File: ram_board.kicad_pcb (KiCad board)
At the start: 4 copper layers, 72.6 x 31.6 mm, 25 parts, among them J1 Bus, J2 PWR, SW1 Config, U1 CPU - Z84C0010AEG, U2 IS61LV5128AL-10TLI, U3 SST39VF040-70-4C-NHE, U4 74LVC2G240, X1 ASV-xxxMHz

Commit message: re-gridded
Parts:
- removed C5: 100nF, Capacitor_SMD:C_0603_1608Metric_Pad1.05x0.95mm_HandSolder
- removed R4, R5, R6, R7, R8, R9: 10K, Resistor_SMD:R_0603_1608Metric_Pad1.05x0.95mm_HandSolder
- removed SW1: Config, Button_Switch_SMD:SW_DIP_SPSTx06_Slide_KingTek_DSHP06TS_W7.62mm_P1.27mm
- X1: value ASV-xxxMHz -> ASV-20MHz
- renumbered C3 to C1, C1 to C2, C2 to C3, U2 to U1, U3 to U2, U1 to U3
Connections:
- C1 pad 1: +3V3 -> Net-(C1-Pad1)
- C2 pad 1: +3V3 -> Net-(C1-Pad1)
- C3 pad 1: +3V3 -> Net-(C1-Pad1)
- C4 pad 1: +3V3 -> Net-(C1-Pad1)
- J1 pad 2: /SW1_5 -> /~RESET
- J1 pad 3: /SW1_3 -> /CLK
- J1 pad 4: /SW1_4 -> /~BUSREQ
- J1 pad 5: /SW1_1 -> /~WAIT
- J1 pad 6: /SW1_2 -> /~IORQ
- J1 pad 8: /SW1_0 -> /~MREQ
- J2 pad 10: (no net) -> /5V
- J2 pad 5: (no net) -> /1V8
- J2 pad 6: (no net) -> /1V8
- J2 pad 7: +3V3 -> VCC
- J2 pad 8: +3V3 -> VCC
- J2 pad 9: (no net) -> /5V
- R1 pad 2: +3V3 -> VCC
- R2 pad 2: +3V3 -> VCC
- R3 pad 2: +3V3 -> VCC
- U1 pad 11: +3V3 -> VCC
- U1 pad 33: +3V3 -> VCC
- U2 pad 32: +3V3 -> VCC
- U3 pad 1: (no net) -> /CLK
- U3 pad 15: (no net) -> /~MREQ
- U3 pad 16: (no net) -> /~IORQ
- U3 pad 21: (no net) -> /~WAIT
- U3 pad 22: (no net) -> /~BUSREQ
- U3 pad 23: (no net) -> /~RESET
- U3 pad 6: (no net) -> VCC
- U4 pad 8: +3V3 -> VCC
- X1 pad 1: (no net) -> VCC
- X1 pad 2: (no net) -> GND
- X1 pad 3: (no net) -> /CLK
- X1 pad 4: (no net) -> VCC
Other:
- board text removed: "1"
- board text removed: "16"
- board text removed: "2"
- board text removed: "32"
- board text removed: "4"
- board text removed: "8"

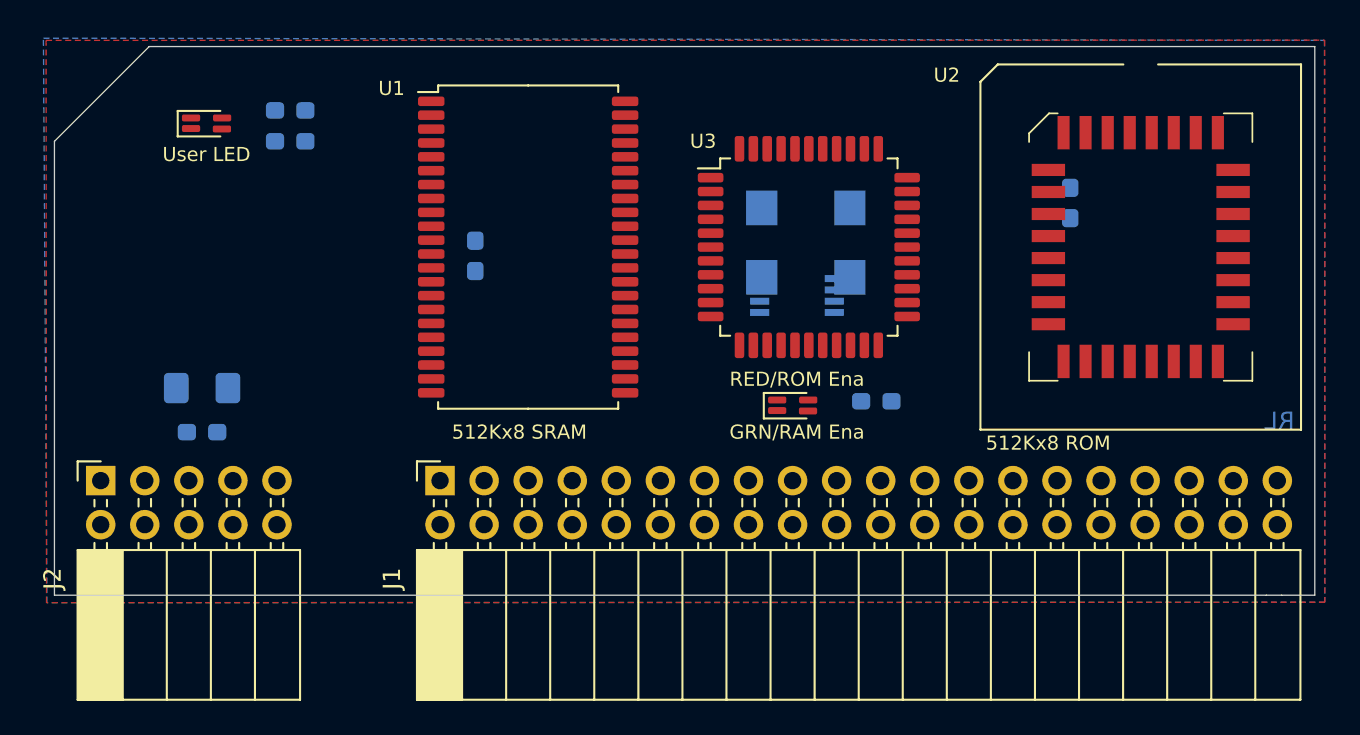
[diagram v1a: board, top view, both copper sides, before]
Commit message: Added plcc socket to library
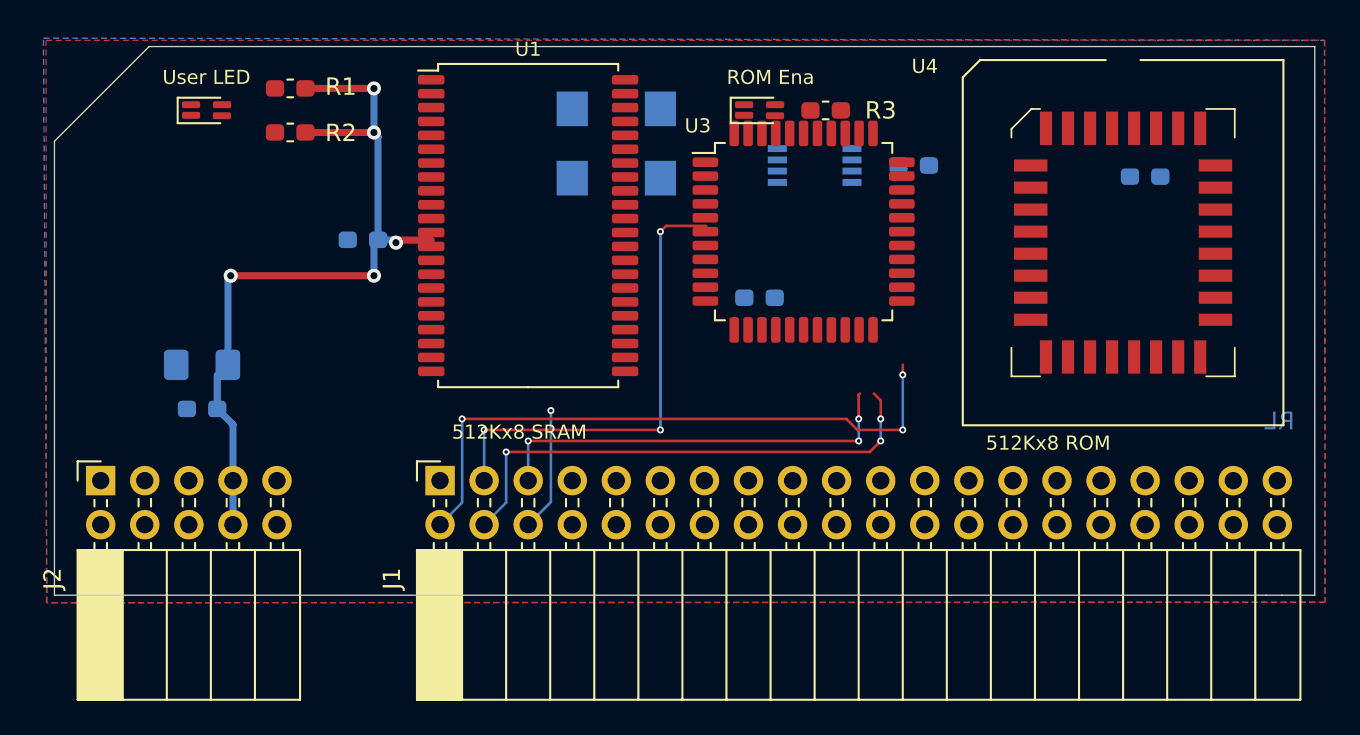
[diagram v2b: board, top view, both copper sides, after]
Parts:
- added C5: 100nF, Capacitor_SMD:C_0603_1608Metric_Pad1.05x0.95mm_HandSolder, B.Cu at (167.0, 79.4)
- added C6: 100nF, Capacitor_SMD:C_0603_1608Metric_Pad1.05x0.95mm_HandSolder, B.Cu at (158.1, 87.0)
- R1, R2, R3: moved to F.Cu
- U1: value IS61LV5128AL-10TLI -> IS61C5128AL-10TLI
- U2: value SST39VF040-70-4C-NHE -> 74LVC2G240; footprint Package_LCC:PLCC-32_SMD-Socket -> Package_SO:TSSOP-8_3x3mm_P0.65mm; moved to B.Cu
- U4: value 74LVC2G240 -> SST39VF040-70-4C-NHE; footprint Package_SO:TSSOP-8_3x3mm_P0.65mm -> ram_rom_brd:PLCC-32_SMD-Socket; moved to F.Cu
- moved G*** 29.6 mm to (137.8, 85.1)
- moved U2 19.4 mm to (161.3, 79.4), turned to 180 degrees
- moved U4 19.0 mm to (179.1, 83.8)
- moved D2 17.1 mm to (158.1, 76.2)
- moved R3 17.0 mm to (161.9, 76.2)
- moved X1 12.3 mm to (149.9, 78.1)
- moved C1 6.54 mm to (135.3, 83.7), turned to 180 degrees
- moved C4 4.58 mm to (180.3, 80.0), turned to 0 degrees
- moved C3 1.34 mm to (126.0, 93.4), turned to 180 degrees
- moved C2 1.34 mm to (126.0, 90.9), turned to 180 degrees
- moved R1 1.27 mm to (131.1, 74.9)
- moved U1 1.24 mm to (144.8, 82.8)
- moved U3 0.94 mm to (160.7, 83.2)
- moved D1 0.76 mm to (126.2, 76.2)
- moved R2 0.51 mm to (131.1, 77.5)
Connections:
- C1 pad 1: Net-(C1-Pad1) -> VCC
- C2 pad 1: Net-(C1-Pad1) -> VCC
- C3 pad 1: Net-(C1-Pad1) -> VCC
- C4 pad 1: Net-(C1-Pad1) -> VCC
- U2 pad 1: /A18 -> /~ENA
- U2 pad 2: /A16 -> /~RAM
- U2 pad 3: /A15 -> Net-(D2-Pad4)
- U2 pad 4: /A12 -> GND
- U2 pad 5: /A7 -> /~ROM
- U2 pad 6: /A6 -> /~ROM
- U2 pad 7: /A5 -> /~ENA
- U2 pad 8: /A4 -> VCC
- U4 pad 1: /~ENA -> /A18
- U4 pad 2: /~RAM -> /A16
- U4 pad 3: Net-(D2-Pad4) -> /A15
- U4 pad 4: GND -> /A12
- U4 pad 5: /~ROM -> /A7
- U4 pad 6: /~ROM -> /A6
- U4 pad 7: /~ENA -> /A5
- U4 pad 8: VCC -> /A4
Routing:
- net VCC: track 0.00 -> 45.4 mm, vias 0 -> 5
- net /~RESET: track 0.00 -> 36.0 mm, vias 0 -> 3
- net /~BUSREQ: track 0.00 -> 29.5 mm, vias 0 -> 3
- net /CLK: track 0.00 -> 27.3 mm, vias 0 -> 3
- net /~WAIT: track 0.00 -> 24.1 mm, vias 0 -> 3
- net /~IORQ: track 0.00 -> 7.12 mm, vias 0 -> 1
- removed copper zone on In1.Cu, net GND
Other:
- copper layers 4 -> 2
- board text added: "ROM Ena"
- board text removed: "GRN/RAM Ena"
- board text removed: "RED/ROM Ena"
